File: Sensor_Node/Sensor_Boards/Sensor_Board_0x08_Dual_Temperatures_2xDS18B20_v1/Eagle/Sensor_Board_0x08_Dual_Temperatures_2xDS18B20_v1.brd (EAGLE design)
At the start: 55 x 35 mm, 16 parts, among them J2 1x3 RA Female .1", J3 1x3 RA Female .1", J4 ARDUINO_ISP, U2 ATMEGA328P_TQFP, Y1 8MHZ

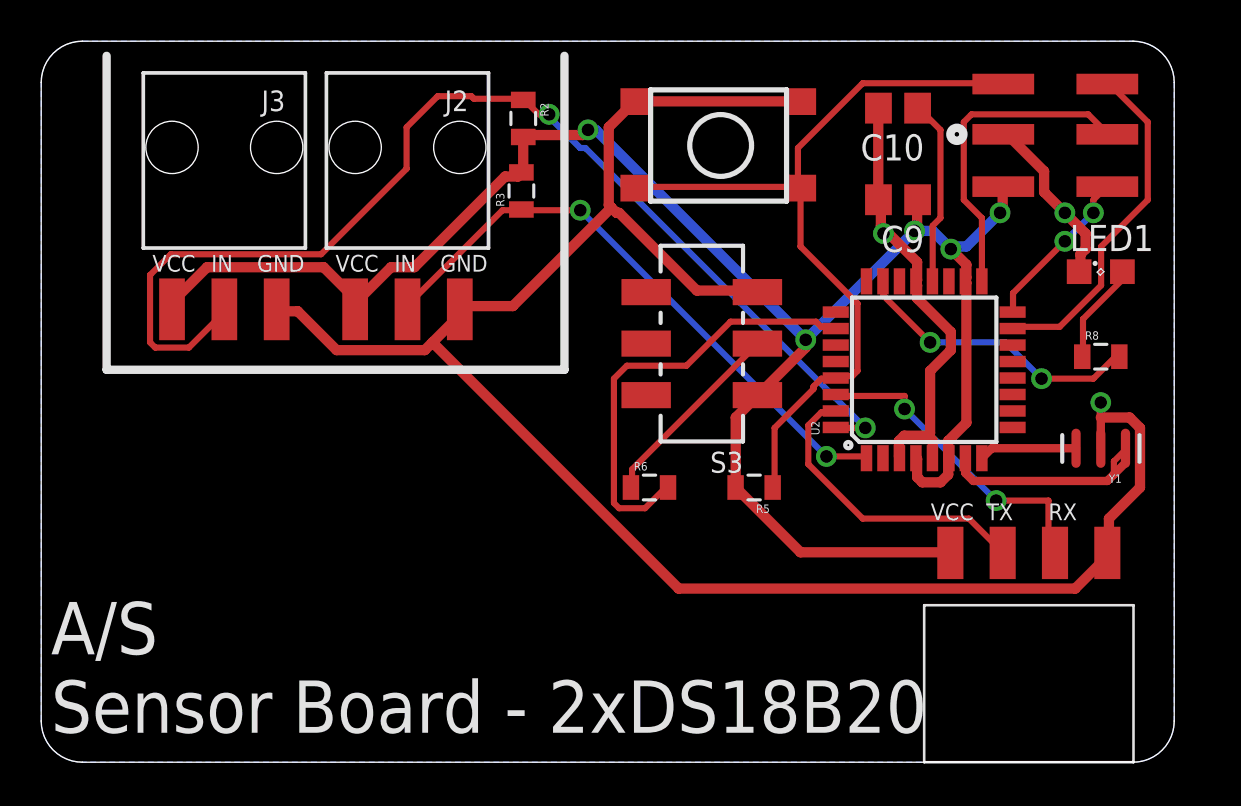
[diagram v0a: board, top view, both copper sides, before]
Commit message: Changes on SensModule 2xDS18B20
- added pogopin programming connector
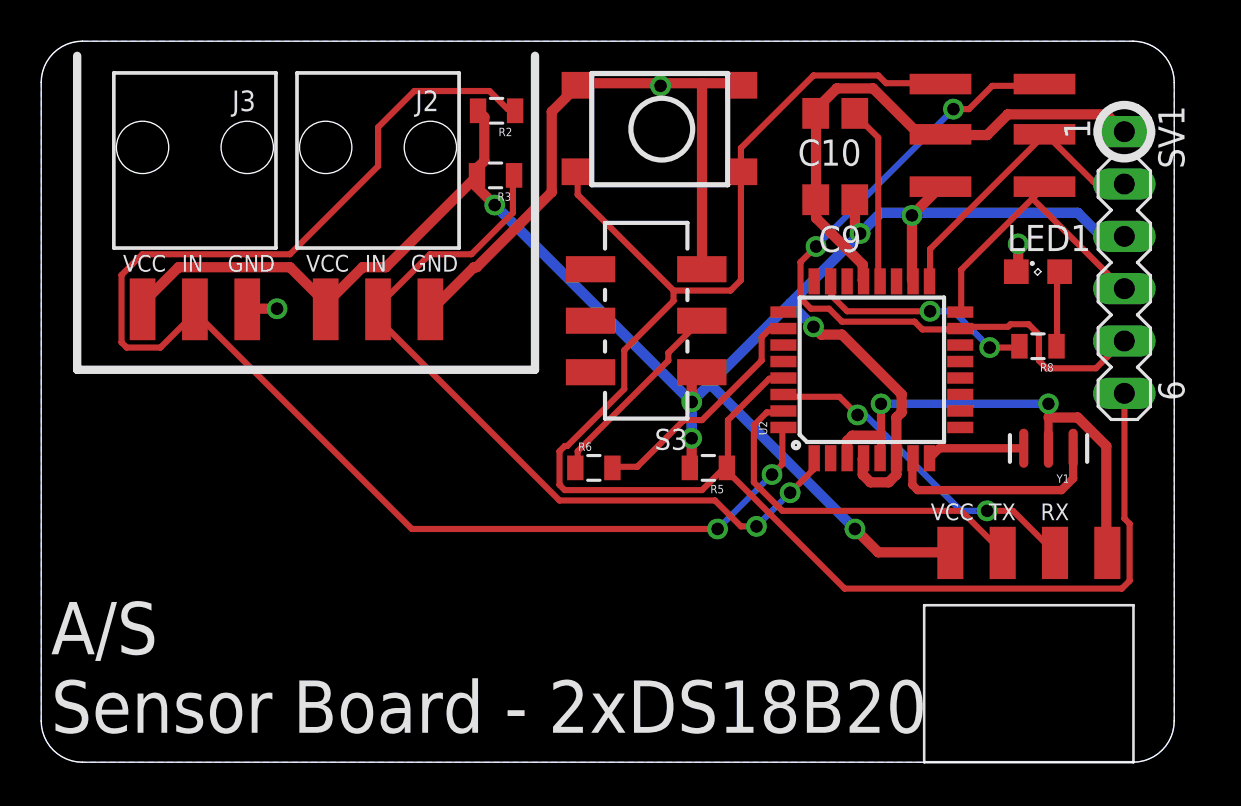
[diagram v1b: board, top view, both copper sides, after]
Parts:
- added SV1: (no value), con-lstb:MA06-1
- moved R8 3.09 mm to (48.4, 20.2), turned to 180 degrees
- moved C10 3.06 mm to (38.5, 31.5)
- moved C9 3.05 mm to (38.5, 27.3)
- moved LED1 3.05 mm to (48.4, 23.8)
- moved J4 3.05 mm to (48.7, 27.9)
- moved S1 2.97 mm to (26.0, 32.9)
- moved S3 2.92 mm to (29.4, 21.4)
- moved R6 2.86 mm to (26.8, 14.3)
- moved U2 2.54 mm to (40.3, 19.1)
- moved Y1 2.54 mm to (48.9, 15.2)
- moved R5 2.42 mm to (32.4, 14.3)
- moved R3 1.47 mm to (22.1, 28.5), turned to 180 degrees
- moved J2 1.43 mm to (16.4, 29.2)
- moved J3 1.43 mm to (7.46, 29.2)
- moved R2 1.35 mm to (22.1, 31.6), turned to 180 degrees
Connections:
- net GND: now also SV1.1
- net MISO: now also SV1.4
- net MOSI: now also SV1.5
- net RESET: now also SV1.6
- net SCK: now also SV1.2
- net VCC: now also SV1.3
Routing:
- net RESET: track 39.5 -> 86.8 mm
- net GND: track 122.5 -> 84.6 mm, vias 3 -> 5
- net MOSI: track 16.8 -> 35.8 mm, vias 0 -> 2
- net VCC: track 92.3 -> 106.3 mm, vias 5 -> 7
- net DS18B20_DATA_1: track 55.6 -> 68.3 mm
- net DBG_ENABLE: track 21.2 -> 11.8 mm
- net DS18B20_DATA_2: track 29.4 -> 38.1 mm
- net MISO: track 8.01 -> 14.1 mm, vias 2 -> 0
- net L1: track 14.3 -> 10.9 mm
- net MCU_TXO: track 14.7 -> 18.0 mm
- net SCK: track 15.6 -> 14.3 mm
- net N$30: track 4.93 -> 3.72 mm
- net MCU_RXI: track 15.7 -> 16.4 mm

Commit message: Changes on all boards
- added capacitor on reset-path
- changed order of pogopin programmer pins

Pulse-Board:
- Deleted input-jumper. Currently one interrupt-pin missing, so print is
not yet routed.
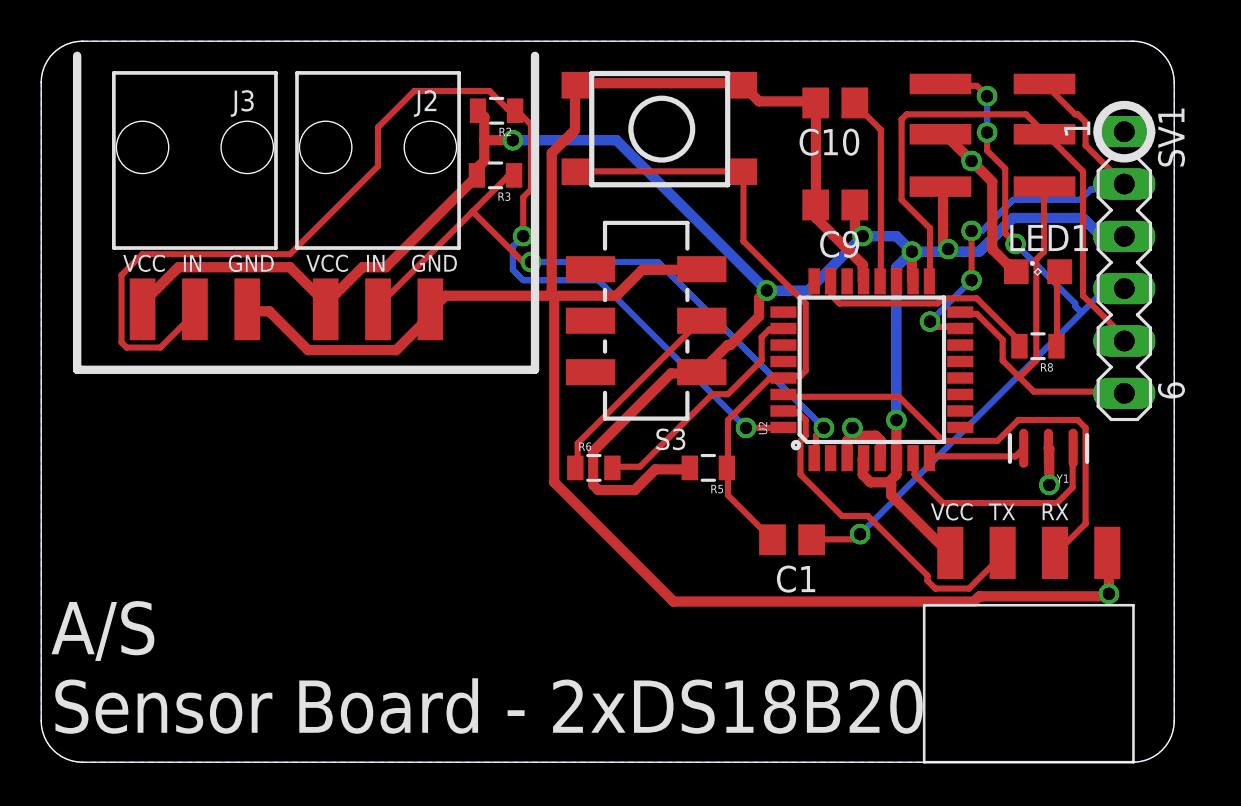
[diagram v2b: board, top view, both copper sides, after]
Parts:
- added C1: 100n, eagle-ltspice:C0805
- moved C10 0.51 mm to (38.5, 32.0)
- moved C9 0.25 mm to (38.5, 27.1)
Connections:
- new net N$4: C1.2, R5.1, S1.3, S1.4, U2.29
- net MISO: now also SV1.6; no longer SV1.4
- net MOSI: now also SV1.2; no longer SV1.5
- net RESET: now also C1.1, SV1.4; no longer R5.1, S1.3, S1.4, SV1.6, U2.29
- net SCK: now also SV1.5; no longer SV1.2
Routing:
- net RESET: track 86.8 -> 35.1 mm, vias 0 -> 4
- net N$4: track 0.00 -> 30.4 mm
- net GND: track 84.6 -> 111.9 mm, vias 5 -> 4
- net MOSI: track 35.8 -> 21.7 mm, vias 2 -> 3
- net SCK: track 14.3 -> 27.6 mm
- net DS18B20_DATA_1: track 68.3 -> 56.9 mm
- net MCU_RXI: track 16.4 -> 22.9 mm, vias 2 -> 0
- net MISO: track 14.1 -> 20.0 mm
- net DS18B20_DATA_2: track 38.1 -> 32.6 mm
- net VCC: track 106.3 -> 105.3 mm, vias 7 -> 6
- net MCU_TXO: track 18.0 -> 17.0 mm
- net N$15: track 8.67 -> 9.19 mm
- net L1: track 10.9 -> 11.2 mm, vias 2 -> 0

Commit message: Finished some boards.
- Minor changes on all boards except
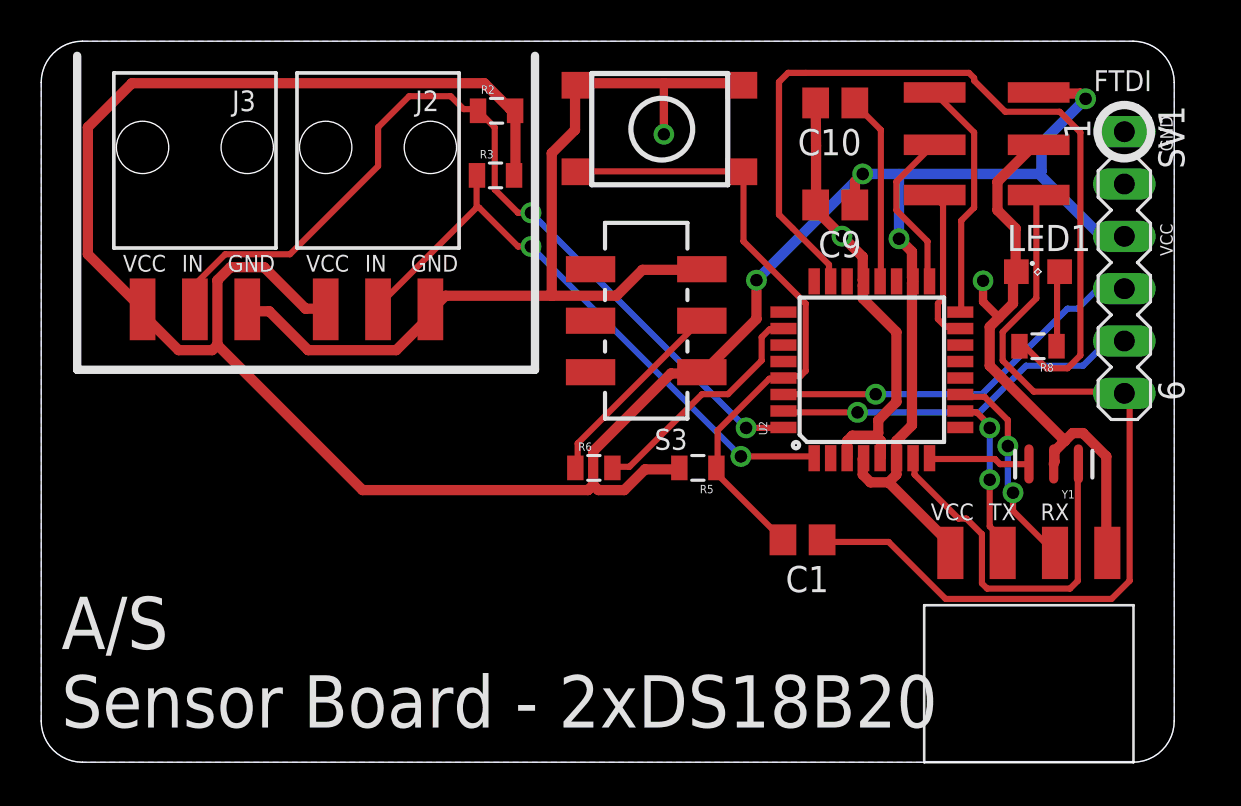
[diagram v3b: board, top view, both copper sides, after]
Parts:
- moved J4 7.03 mm to (43.4, 32.5), turned to 270 degrees
- moved Y1 0.80 mm to (49.1, 14.5)
- moved C1 0.51 mm to (37.0, 10.8)
- moved R5 0.51 mm to (31.9, 14.3)
- turned R2 to 0 degrees
- turned R3 to 0 degrees
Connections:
- new net FTDI_RXI: SV1.4, U2.30
- new net FTDI_TXO: SV1.5, U2.31
- net GND: now also SV1.2
- net MCU_RXI: now also U2.11; no longer U2.30
- net MCU_TXO: now also U2.10; no longer U2.31
- net MISO: no longer SV1.6
- net MOSI: no longer SV1.2
- net RESET: now also SV1.6; no longer SV1.4
- net SCK: no longer SV1.5
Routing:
- net VCC: track 105.3 -> 142.1 mm, vias 6 -> 4
- net L1: track 11.2 -> 41.3 mm
- net SCK: track 27.6 -> 8.11 mm
- net FTDI_RXI: track 0.00 -> 18.7 mm, vias 0 -> 1
- net FTDI_TXO: track 0.00 -> 18.0 mm, vias 0 -> 1
- net GND: track 111.9 -> 96.5 mm, vias 4 -> 3
- net MOSI: track 21.7 -> 7.57 mm, vias 3 -> 0
- net DS18B20_DATA_1: track 56.9 -> 43.1 mm
- net MCU_RXI: track 22.9 -> 10.2 mm, vias 0 -> 2
- net MCU_TXO: track 17.0 -> 8.18 mm, vias 0 -> 2
- net MISO: track 20.0 -> 11.7 mm
- net N$2: track 11.3 -> 18.3 mm
- net RESET: track 35.1 -> 41.0 mm, vias 4 -> 0
- net DS18B20_DATA_2: track 32.6 -> 30.1 mm
- net N$4: track 30.4 -> 31.1 mm
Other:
- board text added: "FTDI"

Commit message: DS18B20 - Board
- adjusted reset path
- minor changes in layout
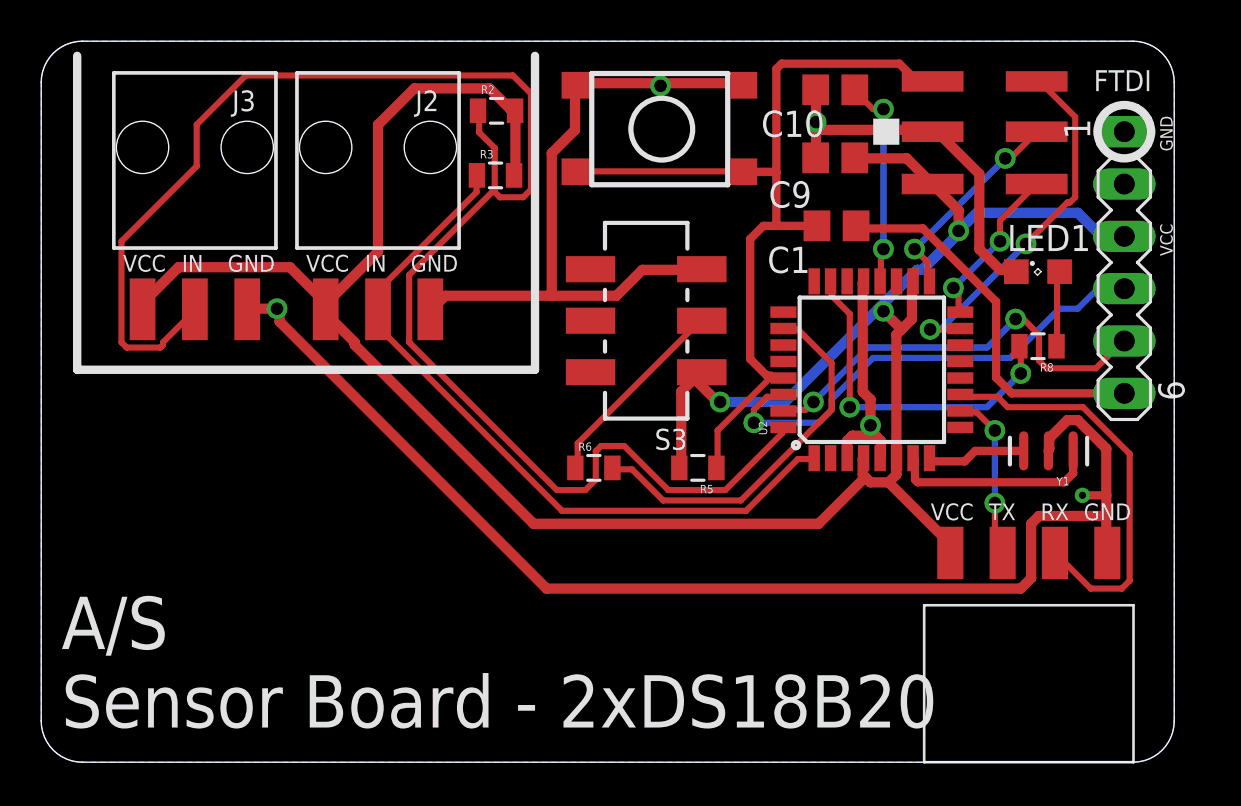
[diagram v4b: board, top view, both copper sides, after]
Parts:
- moved C1 15.3 mm to (38.6, 26.0)
- moved J4 6.66 mm to (48.3, 28.1), turned to 90 degrees
- moved C9 2.29 mm to (38.5, 29.3)
- moved Y1 0.68 mm to (48.9, 15.1)
- moved C10 0.64 mm to (38.5, 32.6)
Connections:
- removed net N$4: C1.2, R5.1, S1.3, S1.4, U2.29
- new net FTDI_RESET: C1.1, SV1.6
- net RESET: now also C1.2, R5.1, S1.3, S1.4, U2.29; no longer C1.1, SV1.6
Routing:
- net DS18B20_DATA_1: track 43.1 -> 79.4 mm, vias 2 -> 0
- net N$4: track 31.1 -> 0.00 mm
- net GND: track 96.5 -> 123.4 mm, vias 3 -> 5
- net L1: track 41.3 -> 16.8 mm, vias 0 -> 2
- net VCC: track 142.1 -> 120.5 mm, vias 4 -> 3
- net FTDI_RESET: track 0.00 -> 18.5 mm
- net MOSI: track 7.57 -> 17.7 mm, vias 0 -> 2
- net MCU_RXI: track 10.2 -> 20.1 mm, vias 2 -> 0
- net N$2: track 18.3 -> 10.1 mm
- net DBG_ENABLE: track 11.8 -> 18.4 mm
- net DS18B20_DATA_2: track 30.1 -> 35.3 mm, vias 2 -> 0
- net FTDI_RXI: track 18.7 -> 23.4 mm
- net MISO: track 11.7 -> 8.05 mm, vias 0 -> 2
- net FTDI_TXO: track 18.0 -> 20.7 mm, vias 1 -> 2
- net SCK: track 8.11 -> 10.2 mm, vias 0 -> 2
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
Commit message: Updated Prototyping Board & DS18B20 Board
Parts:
- removed C10, C9: 100n, eagle-ltspice:C0805
- removed R6: 10k, SparkFun-Passives:0805
- removed R8: 330, SparkFun-Passives:0805
- added C2, C3: 100n, eagle-ltspice:C0805
- added R1: 10k, SparkFun-Passives:0805
- added R4: 4.7k, SparkFun-Passives:0805
- R2: value 4.7k -> 10k
- R3: value 4.7k -> 330
- R5: value 10k -> 4.7k
- moved R3 25.9 mm to (47.0, 21.6), turned to 180 degrees
- moved R2 19.7 mm to (30.2, 13.7), turned to 180 degrees
- moved R5 17.2 mm to (15.2, 18.7)
- moved S3 2.39 mm to (27.0, 21.6)
- moved S1 2.23 mm to (23.8, 33.0)
- moved U2 2.03 mm to (38.7, 17.8)
- moved C1 1.89 mm to (36.8, 25.4)
- moved LED1 1.69 mm to (47.0, 24.8)
- moved U$1 0.95 mm to (43.2, 10.2)
- moved J3 0.79 mm to (6.67, 29.2)
- moved SV1 0.72 mm to (52.1, 24.8)
- moved Y1 0.65 mm to (48.3, 15.2)
- moved J2 0.16 mm to (16.5, 29.2)
- moved J4 0.14 mm to (48.3, 27.9)
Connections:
- net DBG_ENABLE: now also R1.2; no longer R6.2
- net DS18B20_DATA_1: now also R4.1; no longer R2.1
- net DS18B20_DATA_2: now also R5.1; no longer R3.1
- net GND: now also C2.2, C3.2; no longer C10.2, C9.2
- net L1: now also R3.2, U2.14; no longer R8.2, U2.23
- net N$15: now also C3.1; no longer C10.1
- net N$3: now also R1.1; no longer R6.1
- net N$30: now also R3.1; no longer R8.1
- net RESET: now also R2.1; no longer R5.1
- net VCC: now also C2.1, R4.2; no longer C9.1, R3.2
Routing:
- net DS18B20_DATA_1: track 79.4 -> 33.9 mm, vias 0 -> 2
- net GND: track 123.4 -> 80.3 mm, vias 5 -> 7
- net VCC: track 120.5 -> 108.1 mm, vias 3 -> 2
- net L1: track 16.8 -> 5.41 mm, vias 2 -> 0
- net DS18B20_DATA_2: track 35.3 -> 25.9 mm, vias 0 -> 2
- net MCU_TXO: track 8.18 -> 14.4 mm
- net SCK: track 10.2 -> 15.5 mm
- net MISO: track 8.05 -> 13.2 mm
- net N$15: track 10.2 -> 14.8 mm
- net DBG_ENABLE: track 18.4 -> 14.9 mm, vias 0 -> 2
- net N$3: track 9.74 -> 13.1 mm
- net RESET: track 42.3 -> 45.5 mm
- net FTDI_RXI: track 23.4 -> 20.5 mm
- net MCU_RXI: track 20.1 -> 17.8 mm
- net N$2: track 10.1 -> 11.7 mm
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
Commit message: Updated PDFs
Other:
- board text added: "DEBUG"
- board text added: "RESET"
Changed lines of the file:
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@@
 <dimension x1="43.18" y1="10.16" x2="0" y2="10.16" x3="21.59" y3="-6.6675" textsize="1.778" layer="47"/>
 <rectangle x1="40.005" y1="29.845" x2="41.275" y2="31.115" layer="21"/>
+<text x="26.3525" y="26.9875" size="0.8128" layer="21">RESET</text>
+<text x="25.24125" y="15.5575" size="0.8128" layer="21">DEBUG</text>
 </plain>
 <attributes>
